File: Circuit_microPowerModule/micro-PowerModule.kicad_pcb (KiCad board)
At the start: 2 copper layers, 163.7 x 124.2 mm, 231 parts, among them J101 Screw_Terminal_01x02, J102 Jack-DC, J201 USB_C_Receptacle_USB2.0, J202 Debug, J401 Conn_01x03, J402 Screw_Terminal_01x02, J403 Screw_Terminal_01x02, J404 Screw_Terminal_01x02, J501 HDR-2.54 Male 1x5, J502 MikroBus, J503 HDR-2.54 Female 1x5, Q301 MMBT3906, Q302 RK7002BM, Q303 IRF5305S, Q401 RU1C002ZP, Q402 RK7002BM, Q403 RU1C002ZP, Q404 RK7002BM, Q501 S8550, SW201 KMR2, SW301 SW_DPDT_x2, SW501 RotaryEncoder_Switch, U201 W25Q128JVS, U202 RP2040, U204 USBLC6-2P6, U301 OPA376xxDBV, U302 MP2315S, U401 MP2315S, U402 MCP4725xxx-xCH, U403 MT3608, U404 OPA376xxDBV, U405 MCP4725xxx-xCH, U406 INA219BxD, U407 L298N, U408 OPA376xxDBV, U501 MAX485E, Y201 12MHz

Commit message: modify DAC to Voltage follwers
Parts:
- added R423: 0R/5%, Resistor_SMD:R_0603_1608Metric, F.Cu at (94.1, 84.8)
- added R424: 1K/5%, Resistor_SMD:R_0603_1608Metric, F.Cu at (94.1, 87.3)
- added R425: 0R/5%, Resistor_SMD:R_0603_1608Metric, F.Cu at (68.4, 99.7)
- added R426: 1K/5%, Resistor_SMD:R_0603_1608Metric, F.Cu at (68.4, 101.6)
- R416: footprint Resistor_SMD:R_0603_1608Metric -> Resistor_SMD:R_1206_3216Metric
- moved Q403 237.1 mm to (27.7, 90.7)
- moved Q404 237.1 mm to (27.7, 96.2)
- moved C410 221.0 mm to (62.8, 54.8), turned to 90 degrees
- moved R414 218.6 mm to (22.7, 94.2)
- moved C409 216.3 mm to (66.7, 54.8), turned to 90 degrees
- moved C401 213.6 mm to (61.7, 80.8)
- moved C408 212.1 mm to (70.1, 54.7), turned to 90 degrees
- moved U408 210.1 mm to (68.7, 96.0)
- moved C407 208.9 mm to (22.5, 96.5)
- moved U405 201.2 mm to (74.4, 100.7)
- moved C403 191.5 mm to (83.6, 86.9)
- moved U404 189.6 mm to (94.3, 80.7)
- moved R404 183.6 mm to (55.4, 86.8)
- moved R405 183.6 mm to (55.4, 89.3)
- moved D401 178.3 mm to (77.9, 59.2)
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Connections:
- U404 pad 3: Net-(U402-VOUT) -> Net-(U404-+)
- U408 pad 3: Net-(U405-VOUT) -> Net-(U408-+)

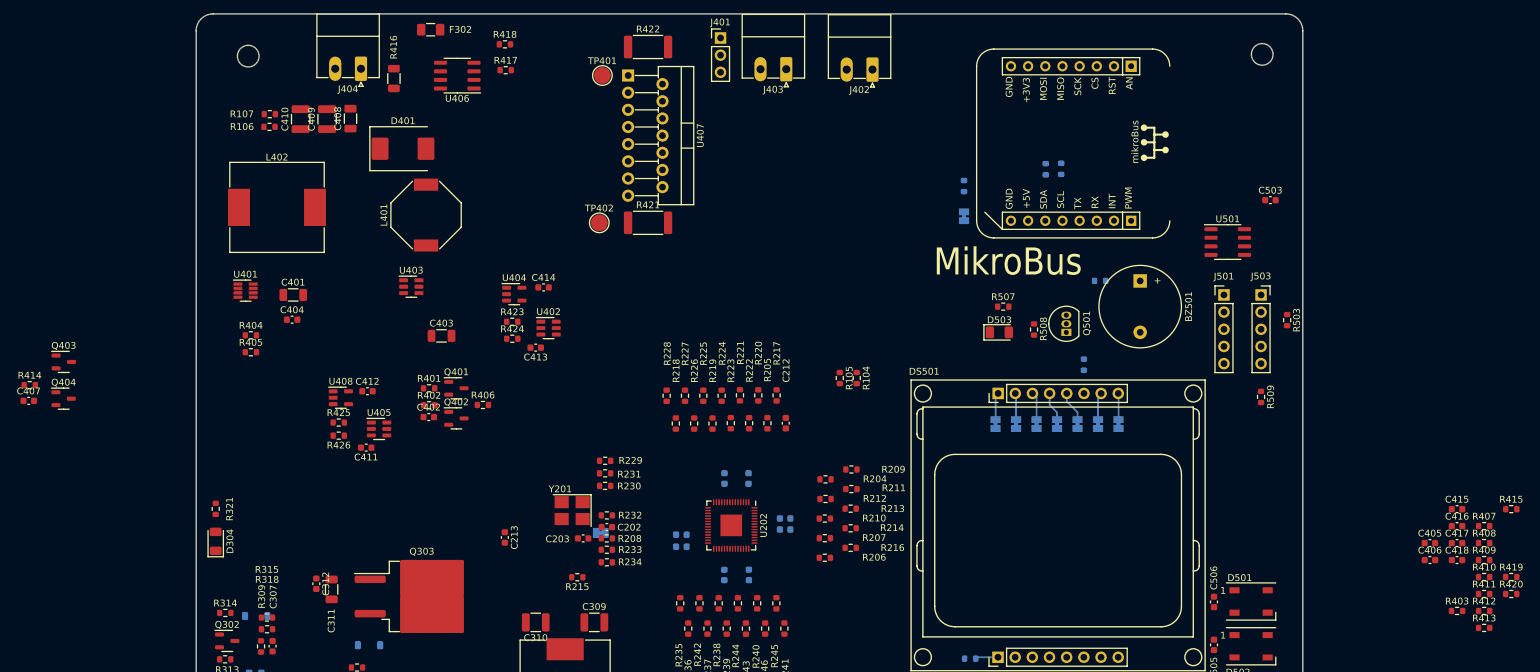
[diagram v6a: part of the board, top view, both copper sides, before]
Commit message: update pcb component layout
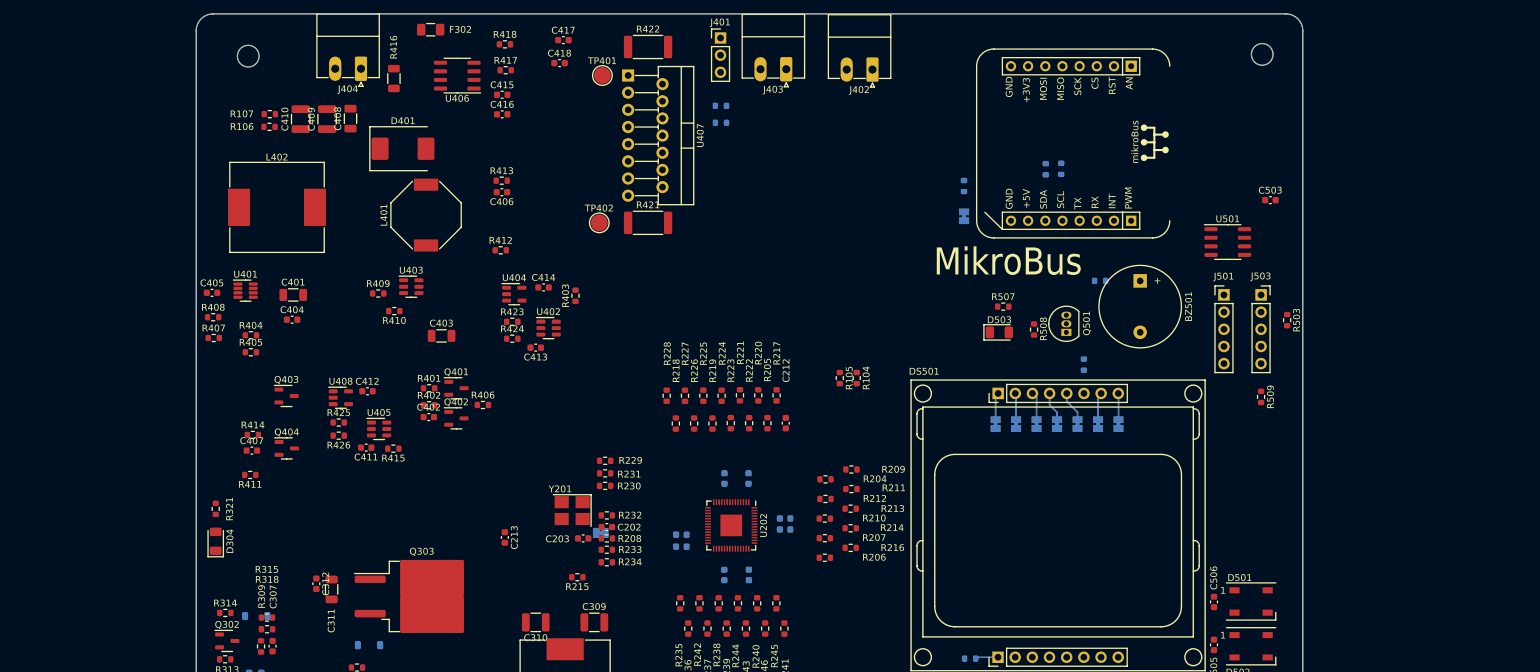
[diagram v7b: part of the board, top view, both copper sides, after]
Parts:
- R419, R420: moved to B.Cu
- moved R408 191.0 mm to (49.8, 84.1)
- moved R407 190.0 mm to (49.9, 87.2)
- moved C405 183.9 mm to (49.6, 80.5)
- moved R411 183.4 mm to (55.3, 107.5), turned to 180 degrees
- moved R409 168.3 mm to (74.2, 80.6)
- moved R410 165.9 mm to (76.6, 83.2), turned to 180 degrees
- moved R415 165.6 mm to (76.5, 103.6), turned to 180 degrees
- moved R413 159.7 mm to (92.5, 63.9)
- moved R412 154.9 mm to (92.4, 74.2)
- moved C415 154.0 mm to (92.6, 51.2)
- moved C416 153.8 mm to (92.6, 54.1)
- moved C418 151.8 mm to (101.1, 46.5)
- moved C417 151.7 mm to (101.6, 43.1)
- moved C406 147.7 mm to (92.5, 65.6), turned to 180 degrees
- moved R403 138.5 mm to (103.4, 80.9), turned to 90 degrees
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
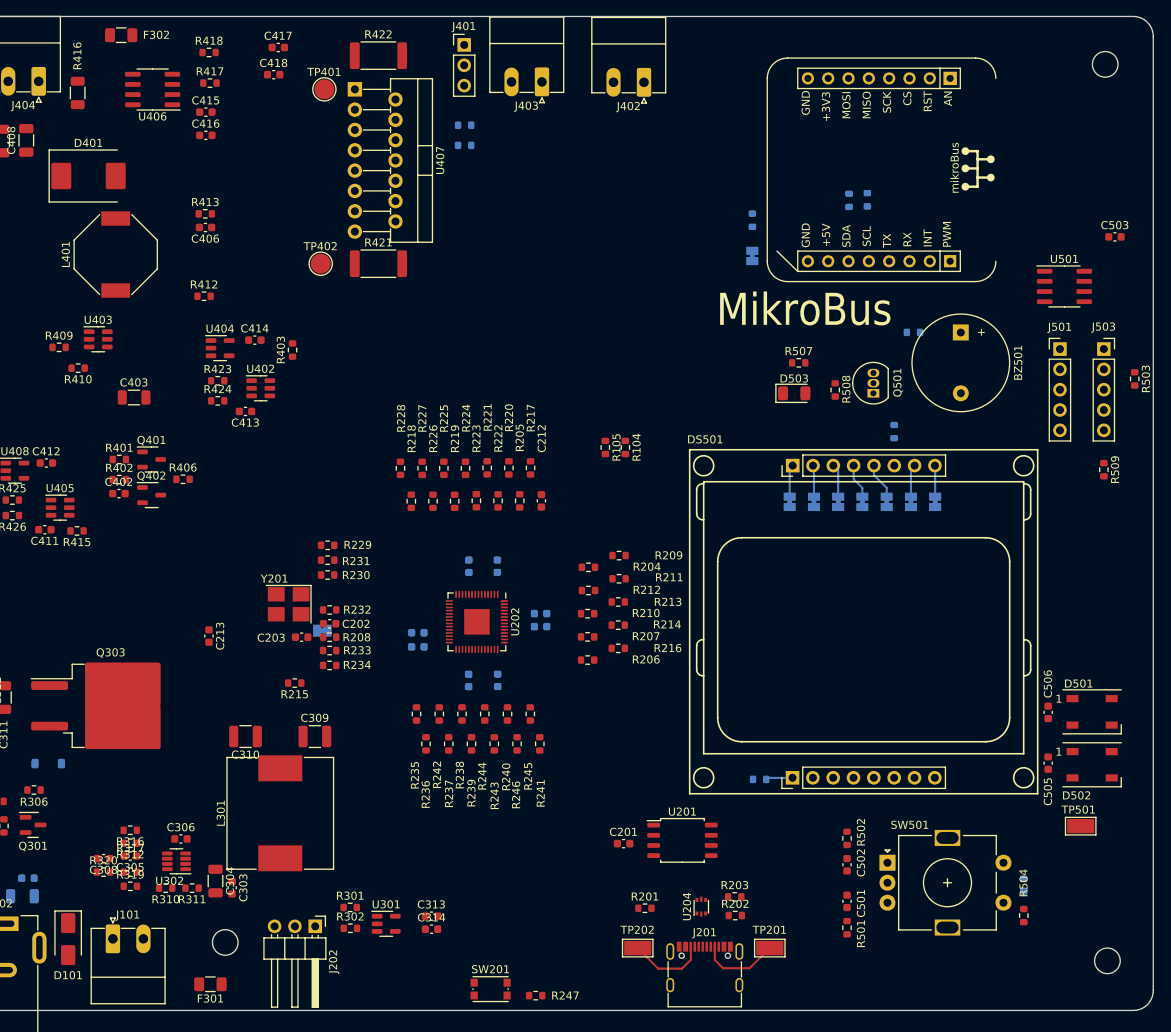
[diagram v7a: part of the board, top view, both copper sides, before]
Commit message: update pcb trace layout
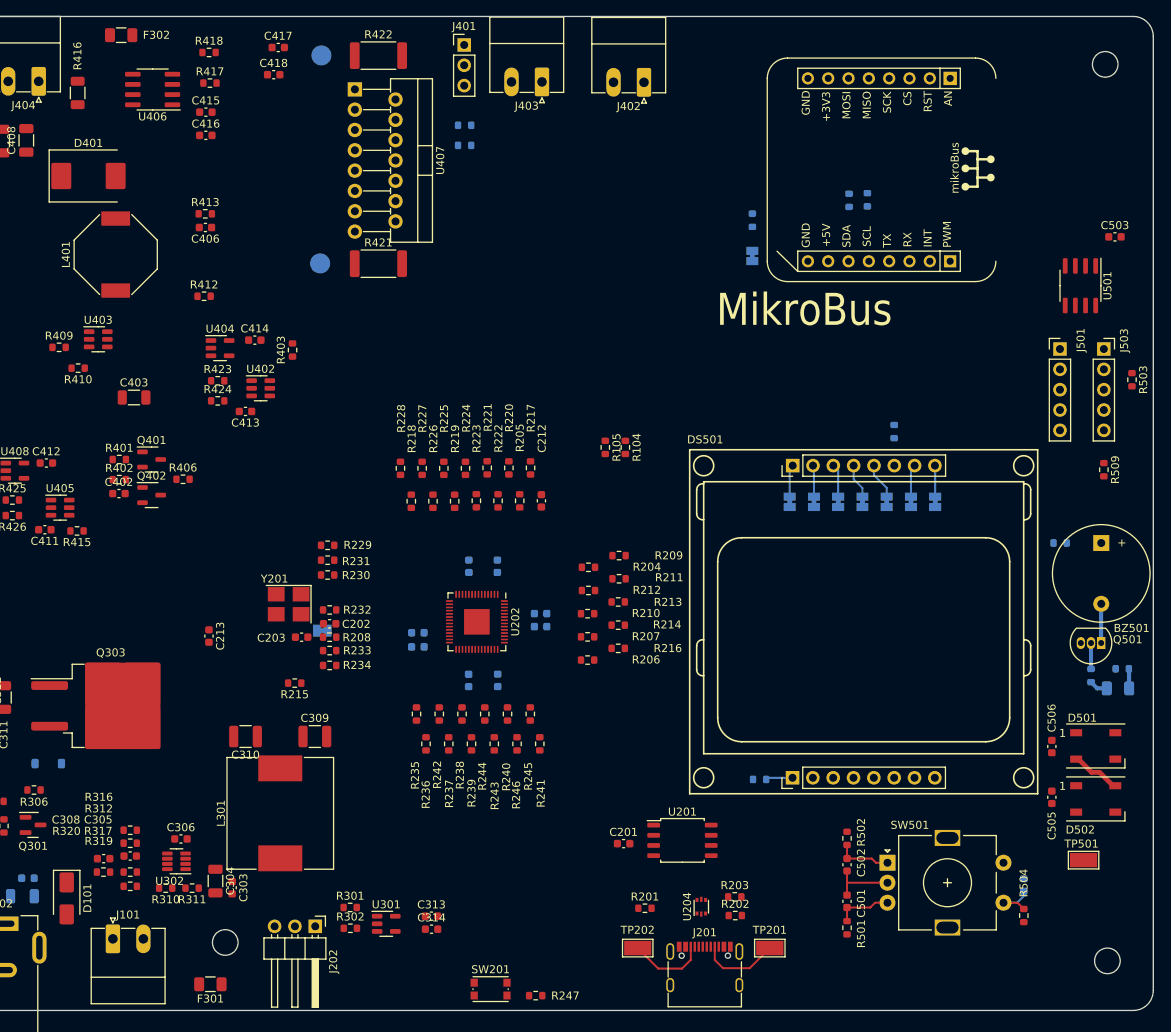
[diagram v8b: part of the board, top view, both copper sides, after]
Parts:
- D503, R507, R508, TP401, TP402: moved to B.Cu
- moved R507 55.7 mm to (207.1, 120.8)
- moved D503 54.8 mm to (206.6, 123.2)
- moved R508 47.9 mm to (203.2, 121.6)
- moved Q501 42.2 mm to (204.5, 117.6), turned to 180 degrees
- moved R510 32.1 mm to (199.3, 105.1)
- moved BZ501 31.6 mm to (204.5, 105.1)
- moved D101 5.09 mm to (75.2, 149.5)
- moved D501 4.29 mm to (203.8, 130.4)
- moved D502 4.29 mm to (203.8, 137.1)
- moved C505 4.29 mm to (198.3, 136.9)
- moved C506 4.29 mm to (198.3, 130.5)
- moved TP501 4.26 mm to (202.3, 144.7)
- moved TP401 4.26 mm to (107.0, 44.1), turned to 180 degrees
- moved U501 2.00 mm to (201.9, 72.9), turned to -90 degrees
- moved R503 0.36 mm to (208.3, 84.7)
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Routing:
- net GNDREF: track 3.89 -> 12.0 mm
- net /RP_ENC_B: track 0.00 -> 7.01 mm
- net /RP_ENC_A: track 0.00 -> 6.98 mm
- net /RP_ENC_SW: track 0.00 -> 6.35 mm
- net Net-(D501-DOUT): track 0.00 -> 6.28 mm
- net Net-(BZ501-+): track 0.00 -> 4.90 mm
- net Net-(Q501-B): track 0.00 -> 3.25 mm
- net Net-(D503-A): track 0.00 -> 2.47 mm
- net /Buzzer_PWM: track 0.00 -> 2.29 mm
